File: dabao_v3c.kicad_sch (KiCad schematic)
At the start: 48 parts, among them J1 USB_C_Receptacle_USB2.0_16P, SW1 SW_Push, SW2 SW_Push, U1 baochip1x, U3 Baochip, U4 MT3406, U5 EMS4000RSW, U6 MT3406, Y2 48.000MHz

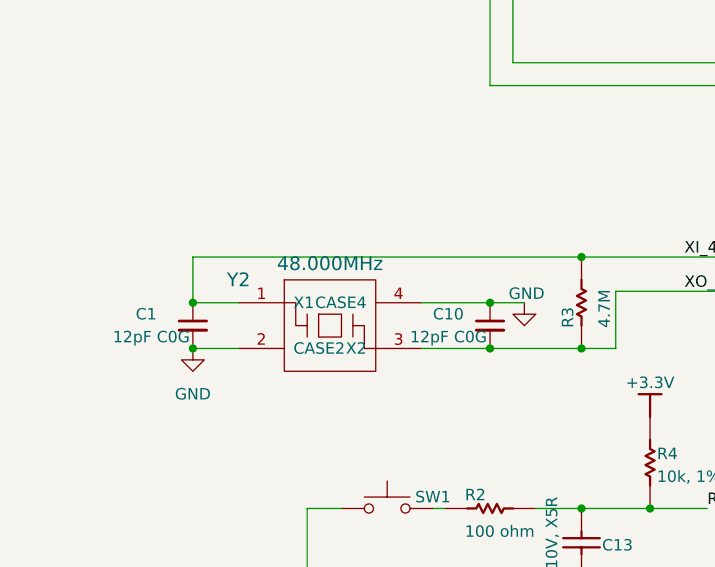
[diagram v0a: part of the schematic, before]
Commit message: update to production release files
add CE/CS logos
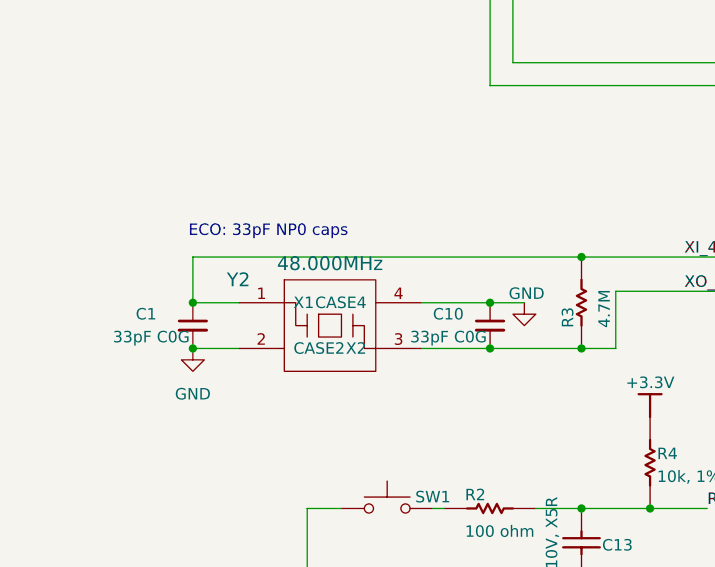
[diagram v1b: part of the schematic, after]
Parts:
- C1, C10: value 12pF C0G -> 33pF C0G; LCSC C277478 -> C56903; MPN CC0201JRNPO9BN120 -> (none); MYPN C-120-50-C0G-0402 -> (none); Rating C0G 50V 0603 -> (none)
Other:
- note added: "ECO: 33pF NP0 caps"
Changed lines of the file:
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@@
 		)
 	)
+	(text "ECO: 33pF NP0 caps"
+		(exclude_from_sim no)
+		(at 54.102 229.616 0)
+		(effects
+			(font
+				(size 1.27 1.27)
+				(color 255 0 17 1)
+			)
+		)
+	)
 	(text "press to toggle bootloader mode (also disconnects USB)"
 		(exclude_from_sim no)
@@
 			)
 		)
-		(property "Value" "12pF C0G"
+		(property "Value" "33pF C0G"
 			(at 69.85 241.3 0)
 			(effects
@@
 			)
 		)
-		(property "Rating" "C0G 50V 0603"
+		(property "Rating" ""
 			(at 78.74 240.03 0)
 			(effects
@@
 			)
 		)
-		(property "MPN" "CC0201JRNPO9BN120"
+		(property "MPN" ""
 			(at 72.39 254 0)
 			(effects
@@
 			)
 		)
-		(property "MYPN" "C-120-50-C0G-0402"
+		(property "MYPN" ""
 			(at 72.39 256.54 0)
 			(effects
@@
 			)
 		)
-		(property "LCSC" "C277478"
+		(property "LCSC" "C56903"
 			(at 72.39 261.62 0)
 			(effects
@@
 			)
 		)
-		(property "Value" "12pF C0G"
+		(property "Value" "33pF C0G"
 			(at 36.83 241.3 0)
 			(effects
@@
 			)
 		)
-		(property "Rating" "C0G 50V 0603"
+		(property "Rating" ""
 			(at 45.72 240.03 0)
 			(effects
@@
 			)
 		)
-		(property "MPN" "CC0201JRNPO9BN120"
+		(property "MPN" ""
 			(at 39.37 254 0)
 			(effects
@@
 			)
 		)
-		(property "MYPN" "C-120-50-C0G-0402"
+		(property "MYPN" ""
 			(at 39.37 256.54 0)
 			(effects
@@
 			)
 		)
-		(property "LCSC" "C277478"
+		(property "LCSC" "C56903"
 			(at 39.37 261.62 0)
 			(effects
